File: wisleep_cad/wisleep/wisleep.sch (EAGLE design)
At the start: 21 parts, among them IC1 STM32F10XCXT6, X1 8MHz

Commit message: pinmapped, some cad, taskified things in lamp
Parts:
- removed JP3: (no value), SparkFun-Connectors:M03X2NO_SILK
- removed LED1: PWR, SparkFunEagle-6-6-07:LED0603
- removed R15: 330, SparkFunEagle-6-6-07:RESISTOR0402
- removed U$6: XC6206OWNOWN, robot:XC6206OWNOWN
- added J1: (no value), con-jack:JACK-PLUG0
- added JP1: M02LOCK, SparkFun-Connectors:M02LOCK
- added MDL1: (no value), ESP8266-ESP12E:ESP8266-12EESP8266-ESP12E
- added U$1: M04X2, SparkFun-Connectors:M04X2
- added U$2: MAX8815AOWNMAX8815A, robot:MAX8815AOWNMAX8815A
- added U1: MAX1555, SparkFun-PowerIC:MAX1555
- C1, C2: value 1uF -> 34pF; device robot:CAP0805 -> robot:CAP0402
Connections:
- net PA0 renamed ACC_INT1
- net PA10 renamed WIFI_RX
- net PA4 renamed SPI_CS
- net PA5 renamed SPI_SCK
- net PA6 renamed SPI_MISO
- net PA7 renamed SPI_MOSI
- net PA8 renamed 5V_ENA
- net PA9 renamed WIFI_TX
- net PB10 renamed SCL
- net PB11 renamed SDA
- net PB15 renamed LAMP_IO
- removed net 5V: C1.1, U$6.VIN
- removed net N$4: LED1.C, R15.1
- removed net PA1: IC1PORTA_L.PA1
- removed net PA15: IC1PORTA_H.PA15
- removed net PB0: IC1PORTB_L.PB0
- removed net PB1: IC1PORTB_L.PB1
- removed net PB12: IC1PORTB_H.PB12
- removed net PB13: IC1PORTB_H.PB13
- removed net PB14: IC1PORTB_H.PB14
- removed net PB2: IC1PORTB_L.PB2
- removed net PB3: IC1PORTB_L.PB3
- removed net PB4: IC1PORTB_L.PB4
- removed net PB5: IC1PORTB_L.PB5
- removed net PB6: IC1PORTB_L.PB6
- removed net PB7: IC1PORTB_L.PB7
- removed net PB8: IC1PORTB_H.PB8
- removed net PB9: IC1PORTB_H.PB9
- removed net PC13: IC1PORTC.PC13
- removed net PC14: IC1PORTC.PC14
- removed net USB_DM: IC1PORTA_H.PA11
- removed net USB_DP: IC1PORTA_H.PA12
- new net GND2: J1.2, JP1.2, U1.GND
- new net N$1: C1.1, IC1PORTC.PC14
- new net N$2: C2.1, IC1PORTC.PC15
- new net N$3: U$2.FB, U$2.POUT1, U$2.POUT2
- new net N$7: U$1.4
- new net POW: J1.3
- new net SWDCLK: U$1.8
- net 3.3V: now also U$1.1; no longer C2.1, JP3.1, LED1.A, U$6.VOUT
- net GND: now also J1.1, U$1.7, U$2.GND, U$2.THERM; no longer JP3.2, R15.2, U$6.GND
- net LED_A: now also IC1PORTC.PC13; no longer IC1PORTC.PC15
- net RST: now also U$1.2
- net SWCLK: no longer JP3.5
- net SWDIO: now also U$1.6; no longer JP3.3
- net USART_RX: now also U$1.5; no longer JP3.6
- net USART_TX: now also U$1.3; no longer JP3.4
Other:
- note added: "BAT+"
- note added: "BAT-"
- note added: "No plug, 1 and 2 connects"
- note added: "POWER"
- note added: "With plug, 1 and 2 breaks"

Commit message: some more cad
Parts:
- removed U1: MAX1555, SparkFun-PowerIC:MAX1555
- added U$3: BQ24072VSON16, robot:BQ24072VSON16
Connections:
- net GND2: no longer U1.GND
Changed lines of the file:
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@@
 <part name="SUPPLY2" library="SparkFun-Aesthetics" deviceset="3.3V" device=""/>
 <part name="GND7" library="SparkFun-Aesthetics" deviceset="GND" device=""/>
-<part name="U1" library="SparkFun-PowerIC" deviceset="MAX1555" device=""/>
 <part name="U$2" library="robot" deviceset="MAX8815A" device="MAX8815A" technology="OWN"/>
 <part name="MDL1" library="ESP8266-ESP12E" deviceset="ESP8266-12E" device="ESP8266-ESP12E"/>
@@
 <part name="GND6" library="SparkFun-Aesthetics" deviceset="GND" device=""/>
 <part name="SUPPLY4" library="supply2" deviceset="GND2" device="" value="BATGND"/>
-<part name="SUPPLY5" library="supply2" deviceset="GND2" device="" value="BATGND"/>
+<part name="U$3" library="robot" deviceset="BQ24072" device="VSON16"/>
 </parts>
 <sheets>
@@
 <instances>
 <instance part="GND7" gate="1" x="71.12" y="149.86"/>
-<instance part="U1" gate="G$1" x="71.12" y="116.84"/>
 <instance part="U$2" gate="G$1" x="71.12" y="170.18"/>
 <instance part="J1" gate="G$1" x="121.92" y="142.24"/>
@@
 <instance part="GND6" gate="1" x="129.54" y="132.08"/>
 <instance part="SUPPLY4" gate="G$1" x="137.16" y="132.08"/>
-<instance part="SUPPLY5" gate="G$1" x="48.26" y="111.76"/>
+<instance part="U$3" gate="G$1" x="71.12" y="78.74"/>
 </instances>
 <busses>
@@
 <junction x="132.08" y="142.24"/>
 </segment>
-<segment>
-<pinref part="U1" gate="G$1" pin="GND"/>
-<pinref part="SUPPLY5" gate="G$1" pin="GND2"/>
-<wire x1="55.88" y1="116.84" x2="48.26" y2="116.84" width="0.127" layer="91"/>
-<wire x1="48.26" y1="116.84" x2="48.26" y2="114.3" width="0.127" layer="91"/>
-</segment>
-</net>
+</net>

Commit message: more cadding
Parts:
- added U$4: MIC5239-3.3v, robot:MIC5239SOT223SOT223
- added U$5: MIC5239-3.3v, robot:MIC5239-8MSOP
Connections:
- net POW renamed POWDC
- removed net GND2: J1.2, JP1.2
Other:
- note removed: "BAT+"
- note removed: "BAT-"
- moved on the sheet: JP1
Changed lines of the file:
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@@
 <part name="JP1" library="SparkFun-Connectors" deviceset="M02" device="LOCK"/>
 <part name="GND6" library="SparkFun-Aesthetics" deviceset="GND" device=""/>
-<part name="SUPPLY4" library="supply2" deviceset="GND2" device="" value="BATGND"/>
 <part name="U$3" library="robot" deviceset="BQ24072" device="VSON16"/>
+<part name="U$4" library="robot" deviceset="MIC5239SOT223" device="SOT223" value="MIC5239-3.3v"/>
+<part name="U$5" library="robot" deviceset="MIC5239-8" device="MSOP" value="MIC5239-3.3v"/>
 </parts>
 <sheets>
@@
 <text x="195.58" y="17.78" size="1.778" layer="94">WISLEEP</text>
 <text x="195.58" y="10.16" size="1.778" layer="94">POWER</text>
-<text x="134.62" y="144.78" size="1.778" layer="97">BAT+</text>
-<text x="134.62" y="142.24" size="1.778" layer="97">BAT-</text>
 <text x="114.3" y="121.92" size="1.778" layer="97">With plug, 1 and 2 breaks</text>
 <text x="114.3" y="124.46" size="1.778" layer="97">No plug, 1 and 2 connects</text>
@@
 <instance part="U$2" gate="G$1" x="71.12" y="170.18"/>
 <instance part="J1" gate="G$1" x="121.92" y="142.24"/>
-<instance part="JP1" gate="G$1" x="147.32" y="144.78" rot="R180"/>
+<instance part="JP1" gate="G$1" x="226.06" y="144.78" rot="R180"/>
 <instance part="GND6" gate="1" x="129.54" y="132.08"/>
-<instance part="SUPPLY4" gate="G$1" x="137.16" y="132.08"/>
 <instance part="U$3" gate="G$1" x="71.12" y="78.74"/>
+<instance part="U$4" gate="G$1" x="154.94" y="96.52"/>
+<instance part="U$5" gate="G$1" x="210.82" y="93.98"/>
 </instances>
 <busses>
@@
 </segment>
 </net>
-<net name="POW" class="0">
+<net name="POWDC" class="0">
 <segment>
 <pinref part="J1" gate="G$1" pin="3"/>
 <wire x1="127" y1="144.78" x2="129.54" y2="144.78" width="0.127" layer="91"/>
-<wire x1="129.54" y1="144.78" x2="139.7" y2="144.78" width="0.127" layer="91"/>
 <wire x1="129.54" y1="144.78" x2="129.54" y2="152.4" width="0.127" layer="91"/>
-<junction x="129.54" y="144.78"/>
 <label x="139.7" y="152.4" size="1.778" layer="95"/>
 <wire x1="129.54" y1="152.4" x2="139.7" y2="152.4" width="0.127" layer="91"/>
 </segment>
 </net>
-<net name="GND2" class="0">
-<segment>
-<pinref part="J1" gate="G$1" pin="2"/>
-<pinref part="JP1" gate="G$1" pin="2"/>
-<wire x1="127" y1="142.24" x2="132.08" y2="142.24" width="0.127" layer="91"/>
-<wire x1="132.08" y1="142.24" x2="139.7" y2="142.24" width="0.127" layer="91"/>
-<wire x1="132.08" y1="142.24" x2="132.08" y2="139.7" width="0.127" layer="91"/>
-<wire x1="132.08" y1="139.7" x2="137.16" y2="139.7" width="0.127" layer="91"/>
-<wire x1="137.16" y1="139.7" x2="137.16" y2="134.62" width="0.127" layer="91"/>
-<pinref part="SUPPLY4" gate="G$1" pin="GND2"/>
-<junction x="132.08" y="142.24"/>
-</segment>
-</net>

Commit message: even moar cad
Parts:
- added C3: 0.1uF, robot:CAP0402
- added C5: 10uF, robot:CAP0402
- added C6: 22uF, robot:CAP_POL1206_CASE-A
- added GY-85: (no value), robot:M08
- added R1, R2, R6, R7: 100k, SparkFunEagle-6-6-07:RESISTOR0402
- added R3, R4, R5, R8: 0, SparkFunEagle-6-6-07:RESISTOR0402
- added U$6: (no value), robot:INDUCTOR3014
- added X2: 32kHz, robot:CRYSTAL
- U$2: value MAX8815AOWNMAX8815A -> MAX8815A10TDFNEP; device robot:MAX8815AOWNMAX8815A -> robot:MAX8815A10TDFNEP
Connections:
- net SPI_MISO renamed N$18
- net SPI_MOSI renamed N$20
- removed net SPI_CS: IC1PORTA_L.PA4
- removed net SPI_SCK: IC1PORTA_L.PA5
- removed net SWDCLK: U$1.8
- new net 5V: R8.1
- new net BAT+: JP1.1, U$3.BAT1, U$3.BAT2
- new net BAT-: JP1.2
- new net G_INT(NC): GY-85.1
- new net M_DRDY(NC): GY-85.3
- new net N$10: U$3.TD
- new net N$11: U$3.ILIM
- new net N$12: U$3.ISET
- new net N$13: R4.2, U$4.OUT
- new net N$14: R5.2, U$5.OUT
- new net N$15: U$2.LX1, U$2.LX2, U$6.2
- new net N$16: R6.1, U$2.OUTS
- new net N$17: IC1PORTA_L.PA1
- new net N$19: R7.2, U$2.SKIPB
- new net N$21: IC1PORTB_H.PB14
- new net N$22: IC1PORTA_H.PA12
- new net N$23: IC1PORTA_H.PA15
- new net N$26: IC1PORTB_L.PB5
- new net N$27: IC1PORTB_L.PB4
- new net N$28: IC1PORTA_H.PA8
- new net N$4: R3.1, U$3.OUT1, U$3.OUT2
- new net N$6: U$3._CE
- new net N$8: U$3.EN1
- new net N$9: U$3.EN2
- new net NCHG: IC1PORTB_H.PB10, R1.2, U$3._CHG
- new net NPGOOD: IC1PORTB_H.PB11, R2.2, U$3._PGOOD
- new net V+: C5.1, R3.2, U$2.BATT, U$4.IN, U$5.IN, U$6.1
- new net VCC: MDL1.VCC, R5.1
- new net WIFI_BL15: IC1PORTB_H.PB13, MDL1.GPIO15
- new net WIFI_BL2: IC1PORTB_L.PB2, MDL1.GPIO2
- new net WIFI_BOOT: IC1PORTB_L.PB0, MDL1.GPIO0
- new net WIFI_ENA: IC1PORTB_H.PB12, MDL1.CH_PD
- new net WIFI_IO4: IC1PORTA_L.PA5, MDL1.GPIO4
- new net WIFI_IO5: IC1PORTA_L.PA4, MDL1.GPIO5
- new net WIFI_POW_ENA: IC1PORTA_H.PA11, U$5.EN
- new net WIFI_RES: IC1PORTB_L.PB1, MDL1.REST
- net 3.3V: now also GY-85.7, R1.1, R2.1, R4.1; no longer LED2.A
- net 5V_ENA: now also IC1PORTB_L.PB3, U$2.ON; no longer IC1PORTA_H.PA8
- net ACC_INT1: now also GY-85.2
- net GND: now also C3.2, C5.2, C6.-, GY-85.6, LED2.C, MDL1.GND, R7.1, U$3.GND, U$3.PAD_GND, U$4.GND@1, U$4.GND@2, U$5.GND@1, U$5.GND@2, U$5.GND@3, U$5.GND@4
- net N$1: now also X2.1
- net N$2: now also X2.2
- net N$3: now also C3.1, C6.+, R6.2, R8.2
- net N$5: now also LED2.A; no longer LED2.C
- net POWDC: now also U$3.IN
- net SCL: now also GY-85.5, IC1PORTB_L.PB6; no longer IC1PORTB_H.PB10
- net SDA: now also GY-85.4, IC1PORTB_L.PB7; no longer IC1PORTB_H.PB11
- net SWCLK: now also U$1.8
- net WIFI_RX: now also MDL1.TXD
- net WIFI_TX: now also MDL1.RXD
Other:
- moved on the sheet: J1, JP1, LED2, U$5

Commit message: cadding soon to an end
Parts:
- removed R5: 0, SparkFunEagle-6-6-07:RESISTOR0402
- added C14, C15, C16, C8, C9: 10uF, robot:CAP0402
- added C4, C7: 22uF, robot:CAP_POL1206_CASE-A
- added JP2, JP3, JP4: M01PTH_LONGPAD, SparkFun-Connectors:M01PTH_LONGPAD
- added NTC1: 10kR, SparkFunEagle-6-6-07:RESISTOR0402
- added R10: 100k, SparkFunEagle-6-6-07:RESISTOR0402
- added R12: 1192R, SparkFunEagle-6-6-07:RESISTOR0402
- added R13: 1113R, SparkFunEagle-6-6-07:RESISTOR0402
- added R14: 22.5kR, SparkFunEagle-6-6-07:RESISTOR0402
- added RSENS_BAT, RSENS_WIFI: 0, SparkFunEagle-6-6-07:RESISTOR0402
- renumbered R3 to RSENS_MAIN, R4 to RSENS_CPU, R8 to RSENS_5V
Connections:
- removed net N$10: U$3.TD
- net 5V: now also JP3.1
- net BAT+: now also C4.+
- net BAT-: now also RSENS_BAT.2
- net GND: now also C14.2, C15.2, C16.2, C4.-, C7.-, C8.2, C9.2, JP4.1, NTC1.2, R12.1, R13.1, R14.1, RSENS_BAT.1, U$3.EN1, U$3.TD, U$3._CE
- net LAMP_IO: now also JP2.1
- net N$11: now also R12.2
- net N$12: now also R13.2
- net N$13: now also C14.1
- net N$14: now also C16.1, RSENS_WIFI.2; no longer R5.2
- net N$6: now also R14.2, U$3.TMR; no longer U$3._CE
- net N$8: now also NTC1.1, U$3.TS; no longer U$3.EN1
- net N$9: now also R10.2
- net POWDC: now also C8.1
- net V+: now also C15.1, C7.+, C9.1, R10.1
- net VCC: now also RSENS_WIFI.1; no longer R5.1

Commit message: wisleep cad rev A - 2 fab
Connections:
- removed net N$18: IC1PORTA_L.PA6
- removed net N$7: U$1.4
- new net DBG_IO: IC1PORTA_L.PA6, U$1.4
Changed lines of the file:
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@@
-</segment>
-</net>
-<net name="N$7" class="0">
-<segment>
-<pinref part="U$1" gate="G$1" pin="4"/>
-<wire x1="261.62" y1="190.5" x2="266.7" y2="190.5" width="0.127" layer="91"/>
 </segment>
 </net>
@@
 </segment>
 </net>
-<net name="N$18" class="0">
+<net name="DBG_IO" class="0">
 <segment>
 <pinref part="IC1" gate="PORTA_L" pin="PA6"/>
 <wire x1="38.1" y1="180.34" x2="33.02" y2="180.34" width="0.127" layer="91"/>
-</segment>
-</net>
+<label x="20.32" y="180.34" size="1.778" layer="95"/>
+</segment>
+<segment>
+<pinref part="U$1" gate="G$1" pin="4"/>
+<wire x1="261.62" y1="190.5" x2="266.7" y2="190.5" width="0.127" layer="91"/>
+<label x="266.7" y="190.5" size="1.778" layer="95"/>
+</segment>
+</net>

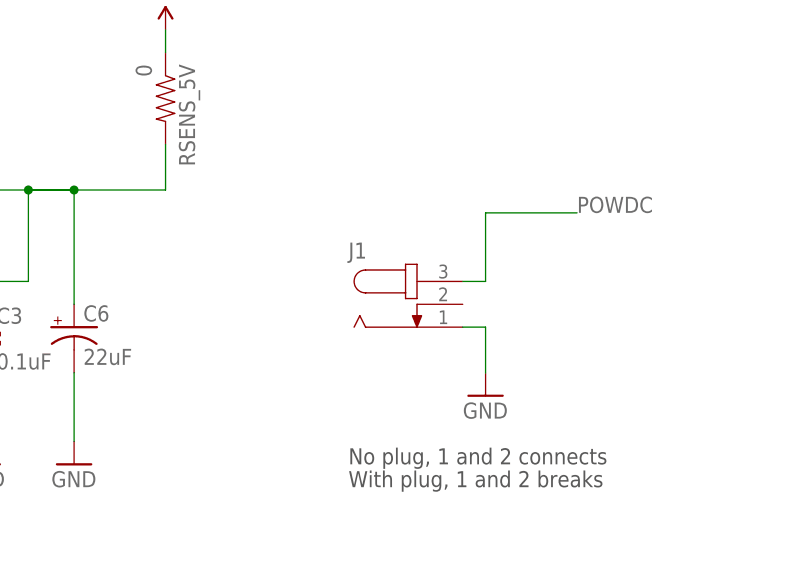
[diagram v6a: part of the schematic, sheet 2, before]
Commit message: fixed up dc jack holes, resent to fab
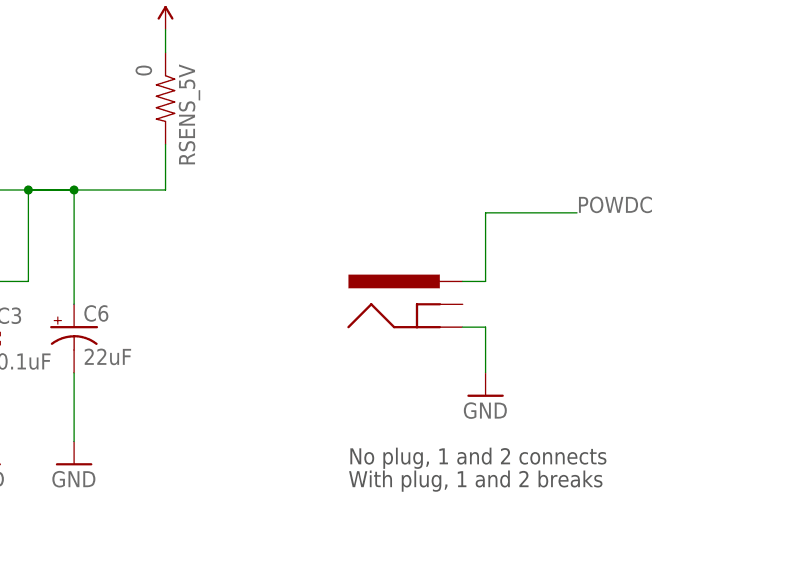
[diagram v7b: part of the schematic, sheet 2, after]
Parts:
- removed J1: (no value), con-jack:JACK-PLUG0
- added U$8: POWER_JACKPTH, SparkFunEagle-6-6-07:POWER_JACKPTH
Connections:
- net GND: now also U$8.GND; no longer J1.1
- net POWDC: now also U$8.PWR; no longer J1.3
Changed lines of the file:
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@@
 <part name="U$2" library="robot" deviceset="MAX8815A" device="10TDFNEP"/>
 <part name="MDL1" library="ESP8266-ESP12E" deviceset="ESP8266-12E" device="ESP8266-ESP12E"/>
-<part name="J1" library="con-jack" deviceset="JACK-PLUG" device="0"/>
 <part name="JP1" library="SparkFun-Connectors" deviceset="M02" device="LOCK"/>
 <part name="GND6" library="SparkFun-Aesthetics" deviceset="GND" device=""/>
@@
 <part name="JP4" library="SparkFun-Connectors" deviceset="M01" device="PTH_LONGPAD"/>
 <part name="GND36" library="SparkFun-Aesthetics" deviceset="GND" device=""/>
+<part name="U$8" library="SparkFunEagle-6-6-07" deviceset="POWER_JACK" device="PTH" value=""/>
 </parts>
 <sheets>
@@
 <instance part="GND7" gate="1" x="71.12" y="147.32"/>
 <instance part="U$2" gate="G$1" x="71.12" y="170.18"/>
-<instance part="J1" gate="G$1" x="154.94" y="165.1"/>
 <instance part="JP1" gate="G$1" x="38.1" y="124.46" rot="R180"/>
 <instance part="GND6" gate="1" x="162.56" y="154.94"/>
@@
 <instance part="RSENS_BAT" gate="G$1" x="73.66" y="124.46" rot="R180"/>
 <instance part="GND35" gate="1" x="83.82" y="119.38"/>
+<instance part="U$8" gate="G$1" x="157.48" y="160.02"/>
 </instances>
 <busses>
@@
 </segment>
 <segment>
-<pinref part="J1" gate="G$1" pin="1"/>
+<pinref part="GND6" gate="1" pin="GND"/>
+<pinref part="U$8" gate="G$1" pin="GND"/>
 <wire x1="160.02" y1="162.56" x2="162.56" y2="162.56" width="0.127" layer="91"/>
 <wire x1="162.56" y1="162.56" x2="162.56" y2="157.48" width="0.127" layer="91"/>
-<pinref part="GND6" gate="1" pin="GND"/>
 </segment>
 <segment>
@@
 <net name="POWDC" class="0">
 <segment>
-<pinref part="J1" gate="G$1" pin="3"/>
+<label x="172.72" y="175.26" size="1.778" layer="95"/>
+<wire x1="162.56" y1="167.64" x2="162.56" y2="175.26" width="0.127" layer="91"/>
+<wire x1="162.56" y1="175.26" x2="172.72" y2="175.26" width="0.127" layer="91"/>
+<pinref part="U$8" gate="G$1" pin="PWR"/>
 <wire x1="160.02" y1="167.64" x2="162.56" y2="167.64" width="0.127" layer="91"/>
-<wire x1="162.56" y1="167.64" x2="162.56" y2="175.26" width="0.127" layer="91"/>
-<label x="172.72" y="175.26" size="1.778" layer="95"/>
-<wire x1="162.56" y1="175.26" x2="172.72" y2="175.26" width="0.127" layer="91"/>
-</segment>
-<segment>
+</segment>
+<segment>
